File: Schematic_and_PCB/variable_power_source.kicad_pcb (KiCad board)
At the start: 2 copper layers, 208 x 105 mm, 56 parts, among them J1 Vout, J10 Pin_16_TL494, J11 Pin_1_TL494, J12 Conn_01x05, J13 Conn_01x05, J14 Conn_01x04, J15 Conn_01x04, J16 LED_connector, J17 LED_connector, J2 Rshunt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

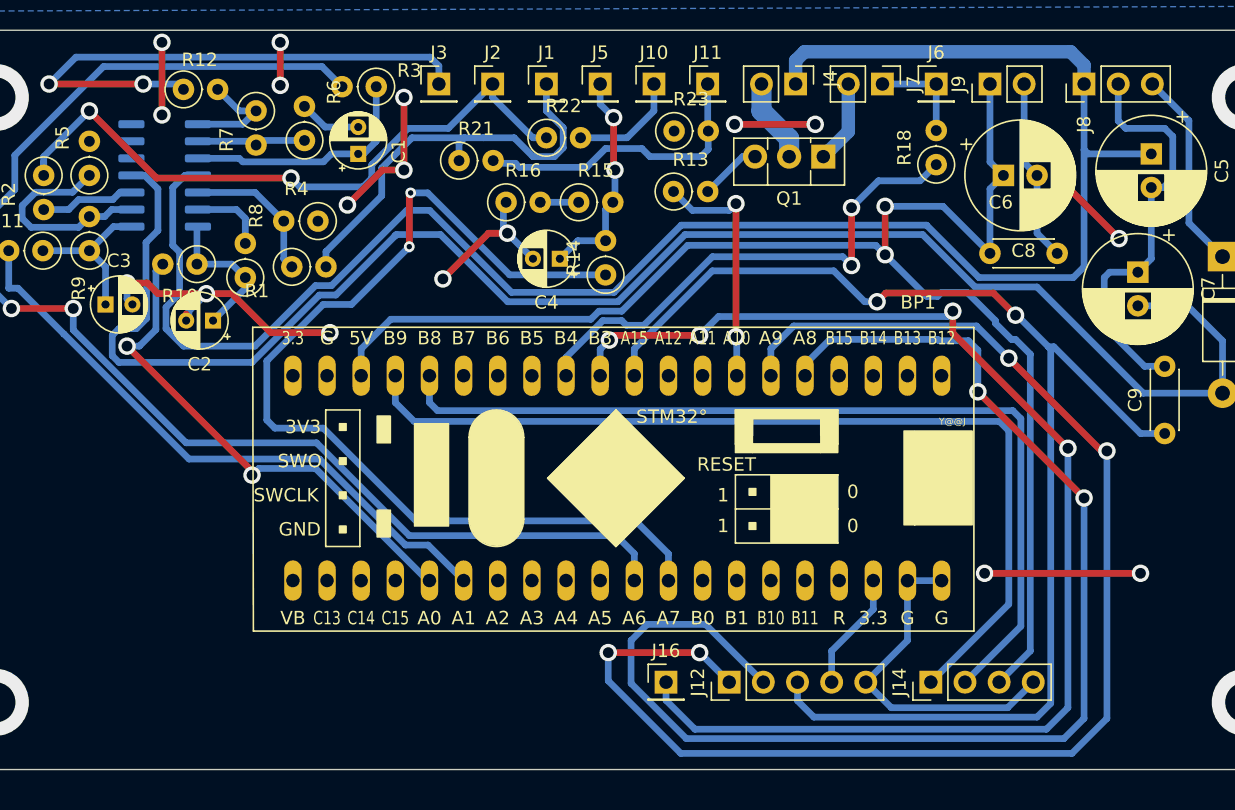
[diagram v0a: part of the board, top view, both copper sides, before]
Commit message: fix pcb errors and add identity mask
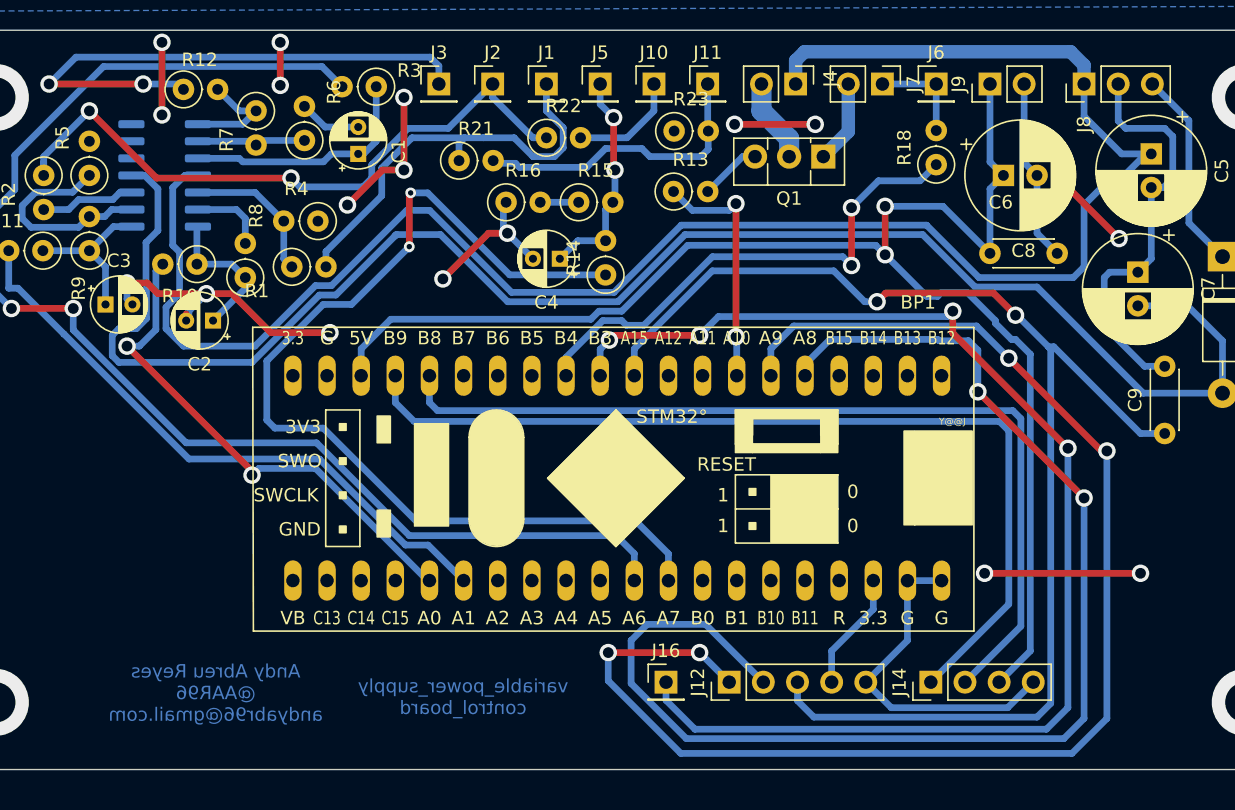
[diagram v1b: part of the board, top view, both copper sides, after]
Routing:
- net +12V: track 137.0 -> 138.0 mm
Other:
- board text added: "Andy Abreu Reyes @AAR96 andyabr96@gmail.com"
- board text added: "variable_power_supply control_board"
